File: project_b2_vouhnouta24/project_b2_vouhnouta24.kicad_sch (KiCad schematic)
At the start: 7 parts, among them J1 AVR-ISP-10, U1 ATmega328-P, Y1 16Mhz

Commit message: custom U1
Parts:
- U1: value ATmega328-P -> ATmega328-P-A
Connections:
- net at R1.1, U1.1 (~{RESET}/PC6): no longer J1.5 (~{RST})
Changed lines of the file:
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@@
 	(paper "A3" portrait)
-	(junction
-		(at 161.29 196.85)
-		(diameter 0)
-		(color 0 0 0 0)
-	)
 	(junction
 		(at 170.18 173.99)
@@
 	(wire
 		(pts
+			(xy 245.11 182.88) (xy 247.65 182.88)
+		)
+		(stroke
+			(width 0)
+			(type default)
+		)
+	)
+	(wire
+		(pts
 			(xy 196.85 196.85) (xy 173.99 196.85)
 		)
@@
 	(wire
 		(pts
-			(xy 161.29 199.39) (xy 228.6 199.39)
+			(xy 245.11 187.96) (xy 247.65 187.96)
 		)
 		(stroke
@@
 	(wire
 		(pts
-			(xy 245.11 190.5) (xy 246.38 190.5)
-		)
-		(stroke
-			(width 0)
-			(type default)
-		)
-	)
-	(wire
-		(pts
-			(xy 246.38 199.39) (xy 236.22 199.39)
-		)
-		(stroke
-			(width 0)
-			(type default)
-		)
-	)
-	(wire
-		(pts
-			(xy 161.29 196.85) (xy 161.29 199.39)
+			(xy 245.11 190.5) (xy 247.65 190.5)
 		)
 		(stroke
@@
 	(wire
 		(pts
-			(xy 161.29 196.85) (xy 166.37 196.85)
+			(xy 160.02 196.85) (xy 166.37 196.85)
 		)
 		(stroke
@@
 	(wire
 		(pts
-			(xy 228.6 203.2) (xy 228.6 199.39)
-		)
-		(stroke
-			(width 0)
-			(type default)
-		)
-	)
-	(wire
-		(pts
-			(xy 236.22 203.2) (xy 228.6 203.2)
-		)
-		(stroke
-			(width 0)
-			(type default)
-		)
-	)
-	(wire
-		(pts
 			(xy 170.18 186.69) (xy 196.85 186.69)
 		)
@@
 	(wire
 		(pts
-			(xy 246.38 199.39) (xy 246.38 190.5)
-		)
-		(stroke
-			(width 0)
-			(type default)
-		)
-	)
-	(wire
-		(pts
 			(xy 170.18 170.18) (xy 170.18 173.99)
 		)
@@
 		)
 	)
-	(wire
-		(pts
-			(xy 236.22 199.39) (xy 236.22 203.2)
-		)
-		(stroke
-			(width 0)
-			(type default)
-		)
-	)
 	(bus
 		(pts
@@
 	(wire
 		(pts
+			(xy 245.11 185.42) (xy 247.65 185.42)
+		)
+		(stroke
+			(width 0)
+			(type default)
+		)
+	)
+	(wire
+		(pts
 			(xy 170.18 176.53) (xy 171.45 176.53)
-		)
-		(stroke
-			(width 0)
-			(type default)
-		)
-	)
-	(wire
-		(pts
-			(xy 160.02 196.85) (xy 161.29 196.85)
 		)
 		(stroke
@@
 			)
 		)
-		(property "Value" "ATmega328-P"
+		(property "Value" "ATmega328-P-A"
 			(at 162.306 150.114 0)
 			(show_name no)

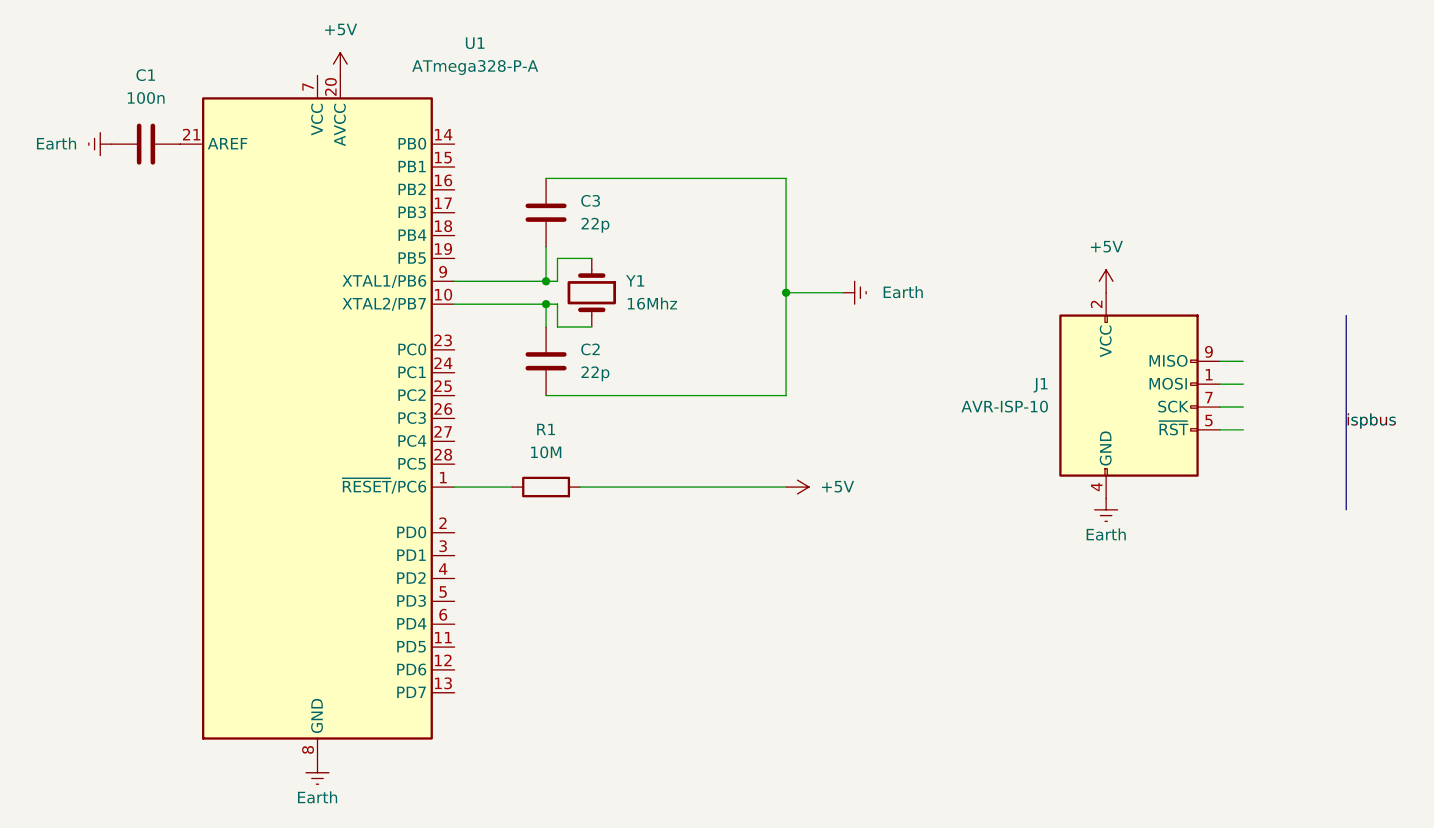
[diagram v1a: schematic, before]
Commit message: implemented U1
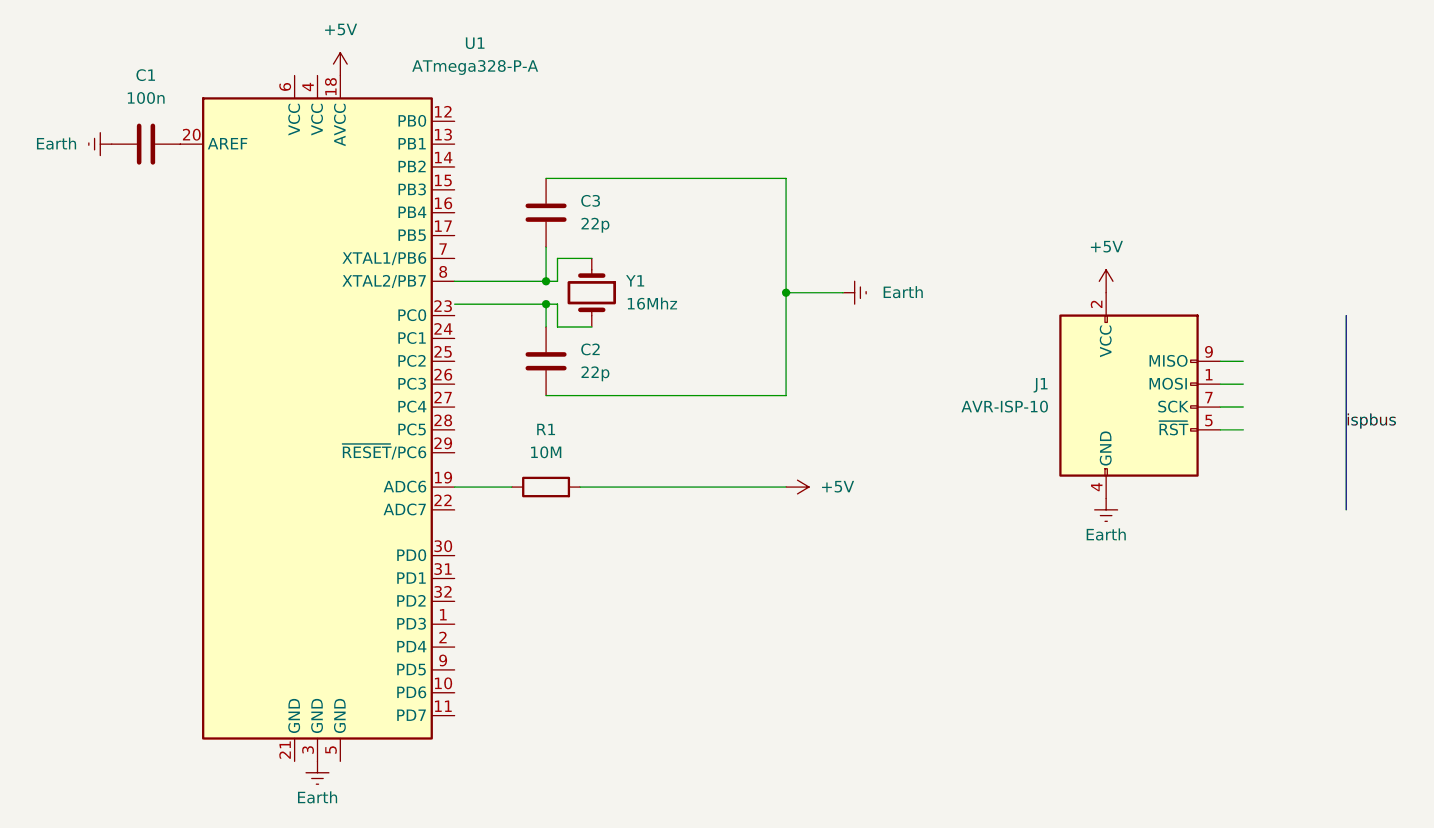
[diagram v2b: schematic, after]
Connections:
- net +5V: now also U1.18 (AVCC); no longer U1.20 (AVCC)
- net Earth: now also U1.3 (GND); no longer U1.8 (GND)
- net at C2.2, Y1.2: no longer U1.10 (XTAL2/PB7)
- net at R1.1: now also U1.19 (ADC6); no longer U1.1 (~{RESET}/PC6)
- net at C3.2, Y1.1: now also U1.8 (XTAL2/PB7); no longer U1.9 (XTAL1/PB6)
- net at C1.1: now also U1.20 (AREF); no longer U1.21 (AREF)
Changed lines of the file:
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@@
 		)
 		(property "Footprint" "Package_DIP:DIP-28_W7.62mm"
-			(at 144.78 189.23 0)
+			(at 77.216 201.422 0)
 			(hide yes)
 			(show_name no)
@@
 		)
 		(property "Datasheet" "http://ww1.microchip.com/downloads/en/DeviceDoc/ATmega328_P%20AVR%20MCU%20with%20picoPower%20Technology%20Data%20Sheet%2040001984A.pdf"
-			(at 144.78 189.23 0)
+			(at 61.722 239.268 0)
 			(hide yes)
 			(show_name no)
@@
 		)
 		(property "Description" "20MHz, 32kB Flash, 2kB SRAM, 1kB EEPROM, DIP-28"
-			(at 144.78 189.23 0)
+			(at 83.312 211.328 0)
 			(hide yes)
 			(show_name no)
@@
 		(pin "4"
 		)
-		(pin "5"
+		(pin "32"
 		)
 		(pin "23"
@@
 		(pin "12"
 		)
-		(pin "6"
+		(pin "30"
 		)
 		(pin "1"
@@
 		(pin "20"
 		)
-		(pin "21"
+		(pin "29"
 		)
 		(pin "16"
@@
 		(pin "9"
 		)
-		(pin "19"
+		(pin "31"
 		)
 		(pin "25"
@@
 		(pin "26"
 		)
+		(pin "6"
+		)
+		(pin "5"
+		)
+		(pin "21"
+		)
+		(pin "19"
+		)
+		(pin "22"
+		)
 		(instances
